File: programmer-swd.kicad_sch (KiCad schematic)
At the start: 3 parts, among them J1 MOLEX, J2 Conn_01x04_Pin, J3 Conn_01x04_Pin

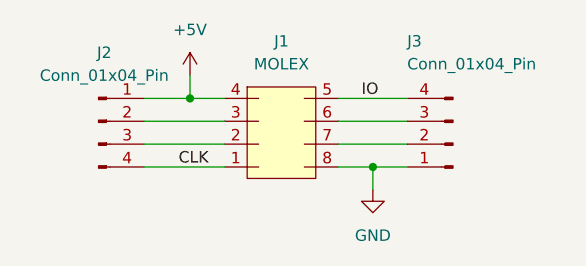
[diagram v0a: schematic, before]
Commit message: Fixed header connections
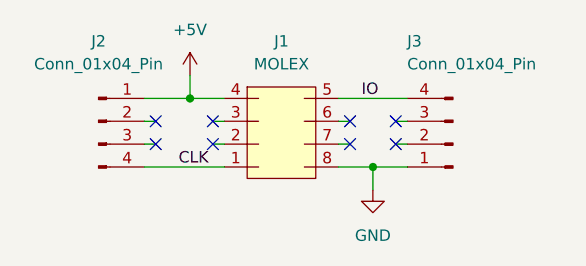
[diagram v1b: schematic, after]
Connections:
- net at J2.2 (Pin_2): no longer J1.3
- net at J2.3 (Pin_3): no longer J1.2
- net at J1.6: no longer J3.3 (Pin_3)
- net at J1.7: no longer J3.2 (Pin_2)
- no-connect marks 0 -> 8
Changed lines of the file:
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@@
   (junction (at 157.48 102.87) (diameter 0) (color 0 0 0 0)
   )
-  (wire (pts (xy 153.67 102.87) (xy 157.48 102.87))
+  (no_connect (at 133.35 97.79))
+  (no_connect (at 154.94 97.79))
+  (no_connect (at 160.02 100.33))
+  (no_connect (at 139.7 97.79))
+  (no_connect (at 160.02 97.79))
+  (no_connect (at 139.7 100.33))
+  (no_connect (at 154.94 100.33))
+  (no_connect (at 133.35 100.33))
+  (wire (pts (xy 160.02 100.33) (xy 161.29 100.33))
     (stroke (width 0) (type default))
   )
-  (wire (pts (xy 153.67 100.33) (xy 161.29 100.33))
+  (wire (pts (xy 139.7 97.79) (xy 140.97 97.79))
+    (stroke (width 0) (type default))
+  )
+  (wire (pts (xy 153.67 102.87) (xy 157.48 102.87))
     (stroke (width 0) (type default))
   )
@@
     (stroke (width 0) (type default))
   )
-  (wire (pts (xy 132.08 97.79) (xy 140.97 97.79))
+  (wire (pts (xy 133.35 100.33) (xy 132.08 100.33))
     (stroke (width 0) (type default))
   )
@@
     (stroke (width 0) (type default))
   )
+  (wire (pts (xy 160.02 97.79) (xy 161.29 97.79))
+    (stroke (width 0) (type default))
+  )
+  (wire (pts (xy 139.7 100.33) (xy 140.97 100.33))
+    (stroke (width 0) (type default))
+  )
   (wire (pts (xy 137.16 92.71) (xy 137.16 95.25))
     (stroke (width 0) (type default))
   )
-  (wire (pts (xy 153.67 97.79) (xy 161.29 97.79))
+  (wire (pts (xy 154.94 97.79) (xy 153.67 97.79))
+    (stroke (width 0) (type default))
+  )
+  (wire (pts (xy 133.35 97.79) (xy 132.08 97.79))
+    (stroke (width 0) (type default))
+  )
+  (wire (pts (xy 154.94 100.33) (xy 153.67 100.33))
     (stroke (width 0) (type default))
   )
   (wire (pts (xy 157.48 102.87) (xy 161.29 102.87))
-    (stroke (width 0) (type default))
-  )
-  (wire (pts (xy 132.08 100.33) (xy 140.97 100.33))
     (stroke (width 0) (type default))
   )
@@
   )
   (symbol (lib_id "Connector:Conn_01x04_Pin") (at 127 97.79 0) (unit 1)
-    (in_bom yes) (on_board yes) (dnp no) (fields_autoplaced)
-    (property "Reference" "J2" (at 127.635 90.17 0)
+    (in_bom yes) (on_board yes) (dnp no)
+    (property "Reference" "J2" (at 127 88.9 0)
       (effects (font (size 1.27 1.27)))
     )
-    (property "Value" "Conn_01x04_Pin" (at 127.635 92.71 0)
+    (property "Value" "Conn_01x04_Pin" (at 127 91.44 0)
       (effects (font (size 1.27 1.27)))
     )
